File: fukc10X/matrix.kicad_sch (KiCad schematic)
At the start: 232 parts

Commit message: Extended Matrix. Added split r-shift and split l-shift. LED support. Removed three of the 4 top right keys because ugly and to make space for indicator leds there
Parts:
- removed D18, D19, D20: D_Small, Diode_SMD:D_SOD-123, symbol Device:D_Small
- removed MX17, MX18, MX19: MX_SW_solder, PCM_marbastlib-mx:SW_MX_1u, symbol PCM_marbastlib-mx:MX_SW_solder
- added D111, D99: D_Small, Diode_SMD:D_SOD-123, symbol Device:D_Small
- added MX115: MX_SW_solder, PCM_marbastlib-mx:SW_MX_1.25u, symbol PCM_marbastlib-mx:MX_SW_solder
- added MX116, MX118: MX_SW_solder, PCM_marbastlib-mx:SW_MX_1u, symbol PCM_marbastlib-mx:MX_SW_solder
- added MX117: MX_SW_solder, PCM_marbastlib-mx:SW_MX_1.75u, symbol PCM_marbastlib-mx:MX_SW_solder
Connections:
- net COL0: now also MX115.1
- net COL10: no longer MX104.1
- net COL11: now also MX104.1, MX116.1; no longer MX105.1
- net COL12: now also MX105.1, MX93.1, MX117.1
- net COL13: now also MX118.1; no longer MX93.1
- net COL6: no longer MX103.1
- net COL7: now also MX103.1
- net ROW4: now also D111.1 (K), D99.1 (K)
- net at D94.2 (A), MX93.2: now also MX117.2
- net at D83.2 (A), MX82.2: now also MX115.2
- new net: D111.2 (A), MX118.2
- new net: D99.2 (A), MX116.2
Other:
- moved on the sheet: D104, D78, MX103, MX77, S1

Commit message: Diodes moved, ISO enter added, Som Silkscreens moved aswell. Generally some cleanup
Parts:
- added D123: D_Small, Diode_SMD:D_SOD-123, symbol Device:D_Small
- added MX119, MX120: MX_SW_solder, PCM_marbastlib-mx:SW_MX_1u, symbol PCM_marbastlib-mx:MX_SW_solder
- added S9: MX_stab, PCM_marbastlib-mx:STAB_MX_ISO, symbol PCM_marbastlib-mx:MX_stab
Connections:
- net COL12: now also MX119.1
- net COL13: now also MX120.1
- net ROW3: now also D123.1 (K)
- net at D78.2 (A), MX77.2: now also MX120.2
- new net: D123.2 (A), MX119.2

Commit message: added split backspace + some updates to the matrix
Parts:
- removed D78: D_Small, Diode_SMD:D_SOD-123, symbol Device:D_Small
- added D124: D_Small, Diode_SMD:D_SOD-123, symbol Device:D_Small
- added MX121, MX122: MX_SW_solder, PCM_marbastlib-mx:SW_MX_1u, symbol PCM_marbastlib-mx:MX_SW_solder
- D10, D100, D101, D102, D103, D104, D105, D106, D107, D108, D109, D11, D110, D111, D112, D113, D114, D115, D12, D123, D13, D14, D15, D16, D17, D2, D21, D22, D23, D24, D25, D26, D27, D28, D29, D3, D30, D31, D32, D33, D34, D35, D36, D37, D38, D39, D4, D40, D41, D42, D43, D44, D45, D46, D47, D48, D49, D5, D50, D51, D52, D53, D54, D55, D56, D57, D58, D59, D6, D60, D61, D62, D64, D65, D67, D68, D69, D7, D70, D71, D72, D73, D74, D75, D76, D77, D79, D8, D80, D81, D82, D83, D84, D85, D86, D87, D88, D89, D9, D90, D91, D92, D93, D94, D95, D96, D97, D98, D99: LCSC (none) -> C81598
- S9: footprint PCM_marbastlib-mx:STAB_MX_ISO -> PCM_marbastlib-mx:STAB_MX_ISO-ROT
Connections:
- net COL12: now also MX77.1
- net COL13: now also MX121.1, MX122.1; no longer MX77.1
- net ROW3: now also D124.1 (K)
- net at D56.2 (A), MX55.2: now also MX120.2
- net at MX77.2: now also D123.2 (A), MX119.2; no longer MX120.2
- net at D35.2 (A), MX34.2: now also MX121.2
- new net: D124.2 (A), MX122.2
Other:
- moved on the sheet: MX120, MX77, S5

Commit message: silkscreen adjustment. 87U bottom row with 6u spacebar added.
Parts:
- added D125: D_Small, Diode_SMD:D_SOD-123, symbol Device:D_Small
- added MX123: MX_SW_solder, PCM_marbastlib-mx:SW_MX_1.5u, symbol PCM_marbastlib-mx:MX_SW_solder
- added MX124, MX125: MX_SW_solder, PCM_marbastlib-mx:SW_MX_1u, symbol PCM_marbastlib-mx:MX_SW_solder
- added S10: MX_stab, PCM_marbastlib-mx:STAB_MX_6u, symbol PCM_marbastlib-mx:MX_stab
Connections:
- net COL10: now also MX123.1
- net COL11: now also MX124.1
- net COL7: now also MX125.1
- net ROW5: now also D125.1 (K)
- net at D105.2 (A), MX104.2: now also MX124.2
- net at D104.2 (A), MX103.2: now also MX125.2
- new net: D125.2 (A), MX123.2
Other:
- moved on the sheet: S2

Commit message: adjusted spare diodes and some rounting. Updated step and production files
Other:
- moved on the sheet: S10
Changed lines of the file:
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@@
 	)
 	(junction
-		(at 41.91 130.81)
-		(diameter 0)
-		(color 0 0 0 0)
-	)
-	(junction
 		(at 120.65 33.02)
 		(diameter 0)
@@
 	)
 	(junction
-		(at 64.77 125.73)
-		(diameter 0)
-		(color 0 0 0 0)
-	)
-	(junction
 		(at 299.72 100.33)
 		(diameter 0)
@@
 	)
 	(junction
-		(at 36.83 125.73)
-		(diameter 0)
-		(color 0 0 0 0)
-	)
-	(junction
 		(at 111.76 118.11)
 		(diameter 0)
@@
 	)
 	(junction
-		(at 50.8 125.73)
-		(diameter 0)
-		(color 0 0 0 0)
-	)
-	(junction
 		(at 162.56 90.17)
 		(diameter 0)
@@
 	)
 	(junction
-		(at 181.61 130.81)
-		(diameter 0)
-		(color 0 0 0 0)
-	)
-	(junction
 		(at 153.67 100.33)
 		(diameter 0)
@@
 	)
 	(junction
-		(at 209.55 130.81)
-		(diameter 0)
-		(color 0 0 0 0)
-	)
-	(junction
 		(at 195.58 64.77)
 		(diameter 0)
@@
 	)
 	(junction
-		(at 218.44 125.73)
-		(diameter 0)
-		(color 0 0 0 0)
-	)
-	(junction
 		(at 176.53 33.02)
 		(diameter 0)
@@
 	)
 	(junction
-		(at 223.52 130.81)
-		(diameter 0)
-		(color 0 0 0 0)
-	)
-	(junction
 		(at 134.62 72.39)
 		(diameter 0)
@@
 	)
 	(junction
-		(at 55.88 130.81)
-		(diameter 0)
-		(color 0 0 0 0)
-	)
-	(junction
 		(at 190.5 107.95)
 		(diameter 0)
@@
 	)
 	(junction
-		(at 176.53 125.73)
-		(diameter 0)
-		(color 0 0 0 0)
-	)
-	(junction
 		(at 294.64 107.95)
 		(diameter 0)
@@
 	)
 	(junction
-		(at 69.85 130.81)
-		(diameter 0)
-		(color 0 0 0 0)
-	)
-	(junction
 		(at 270.51 33.02)
 		(diameter 0)
@@
 	)
 	(junction
-		(at 204.47 125.73)
-		(diameter 0)
-		(color 0 0 0 0)
-	)
-	(junction
 		(at 83.82 64.77)
 		(diameter 0)
@@
 	(wire
 		(pts
-			(xy 55.88 130.81) (xy 62.23 130.81)
-		)
-		(stroke
-			(width 0)
-			(type default)
-		)
-	)
-	(wire
-		(pts
 			(xy 139.7 64.77) (xy 153.67 64.77)
 		)
@@
 	(wire
 		(pts
-			(xy 176.53 130.81) (xy 181.61 130.81)
-		)
-		(stroke
-			(width 0)
-			(type default)
-		)
-	)
-	(wire
-		(pts
 			(xy 190.5 54.61) (xy 190.5 72.39)
 		)
@@
 	(wire
 		(pts
-			(xy 190.5 130.81) (xy 195.58 130.81)
-		)
-		(stroke
-			(width 0)
-			(type default)
-		)
-	)
-	(wire
-		(pts
 			(xy 313.69 82.55) (xy 327.66 82.55)
 		)
@@
 	(wire
 		(pts
-			(xy 171.45 125.73) (xy 176.53 125.73)
-		)
-		(stroke
-			(width 0)
-			(type default)
-		)
-	)
-	(wire
-		(pts
 			(xy 190.5 125.73) (xy 196.85 125.73)
 		)
@@
 	(wire
 		(pts
-			(xy 223.52 130.81) (xy 229.87 130.81)
-		)
-		(stroke
-			(width 0)
-			(type default)
-		)
-	)
-	(wire
-		(pts
 			(xy 167.64 82.55) (xy 181.61 82.55)
 		)
@@
 	(wire
 		(pts
-			(xy 209.55 130.81) (xy 215.9 130.81)
-		)
-		(stroke
-			(width 0)
-			(type default)
-		)
-	)
-	(wire
-		(pts
 			(xy 36.83 21.59) (xy 36.83 33.02)
 		)
@@
 	(wire
 		(pts
-			(xy 204.47 125.73) (xy 210.82 125.73)
-		)
-		(stroke
-			(width 0)
-			(type default)
-		)
-	)
-	(wire
-		(pts
 			(xy 299.72 64.77) (xy 313.69 64.77)
 		)
@@
 	(wire
 		(pts
-			(xy 50.8 125.73) (xy 57.15 125.73)
-		)
-		(stroke
-			(width 0)
-			(type default)
-		)
-	)
-	(wire
-		(pts
 			(xy 64.77 72.39) (xy 64.77 90.17)
 		)
@@
 	(wire
 		(pts
-			(xy 64.77 125.73) (xy 71.12 125.73)
-		)
-		(stroke
-			(width 0)
-			(type default)
-		)
-	)
-	(wire
-		(pts
 			(xy 204.47 107.95) (xy 204.47 125.73)
 		)
@@
 	(wire
 		(pts
-			(xy 127 125.73) (xy 134.62 125.73)
-		)
-		(stroke
-			(width 0)
-			(type default)
-		)
-	)
-	(wire
-		(pts
 			(xy 242.57 21.59) (xy 242.57 33.02)
 		)
@@
 	(wire
 		(pts
-			(xy 218.44 125.73) (xy 224.79 125.73)
-		)
-		(stroke
-			(width 0)
-			(type default)
-		)
-	)
-	(wire
-		(pts
 			(xy 64.77 90.17) (xy 64.77 107.95)
 		)
@@
 	(wire
 		(pts
-			(xy 69.85 130.81) (xy 76.2 130.81)
-		)
-		(stroke
-			(width 0)
-			(type default)
-		)
-	)
-	(wire
-		(pts
 			(xy 162.56 72.39) (xy 162.56 90.17)
 		)
@@
 	(wire
 		(pts
-			(xy 185.42 125.73) (xy 190.5 125.73)
-		)
-		(stroke
-			(width 0)
-			(type default)
-		)
-	)
-	(wire
-		(pts
 			(xy 195.58 82.55) (xy 209.55 82.55)
 		)
@@
 	(wire
 		(pts
-			(xy 132.08 130.81) (xy 139.7 130.81)
-		)
-		(stroke
-			(width 0)
-			(type default)
-		)
-	)
-	(wire
-		(pts
 			(xy 181.61 82.55) (xy 195.58 82.55)
 		)
@@
 	(wire
 		(pts
-			(xy 41.91 130.81) (xy 46.99 130.81)
-		)
-		(stroke
-			(width 0)
-			(type default)
-		)
-	)
-	(wire
-		(pts
 			(xy 55.88 135.89) (xy 69.85 135.89)
 		)
@@
 	(wire
 		(pts
-			(xy 36.83 125.73) (xy 41.91 125.73)
-		)
-		(stroke
-			(width 0)
-			(type default)
-		)
-	)
-	(wire
-		(pts
 			(xy 83.82 64.77) (xy 97.79 64.77)
 		)
@@
 	(symbol
 		(lib_id "PCM_marbastlib-mx:MX_stab")
-		(at 152.4 146.05 0)
+		(at 118.11 128.27 0)
 		(unit 1)
 		(body_style 1)
@@
 		(fields_autoplaced yes)
 		(property "Reference" "S10"
-			(at 158.75 144.6529 0)
+			(at 124.46 126.8729 0)
 			(show_name no)
 			(do_not_autoplace no)
@@
 		)
 		(property "Value" "MX_stab"
-			(at 158.75 147.1929 0)
+			(at 124.46 129.4129 0)
 			(show_name no)
 			(do_not_autoplace no)
@@
 		)
 		(property "Footprint" "PCM_marbastlib-mx:STAB_MX_6u"
-			(at 152.4 146.05 0)
+			(at 118.11 128.27 0)
 			(hide yes)
 			(show_name no)
@@
 		)
 		(property "Datasheet" ""
-			(at 152.4 146.05 0)
+			(at 118.11 128.27 0)
 			(hide yes)
 			(show_name no)
@@
 		)
 		(property "Description" "Cherry MX-style stabilizer"
-			(at 152.4 146.05 0)
+			(at 118.11 128.27 0)
 			(hide yes)
 			(show_name no)

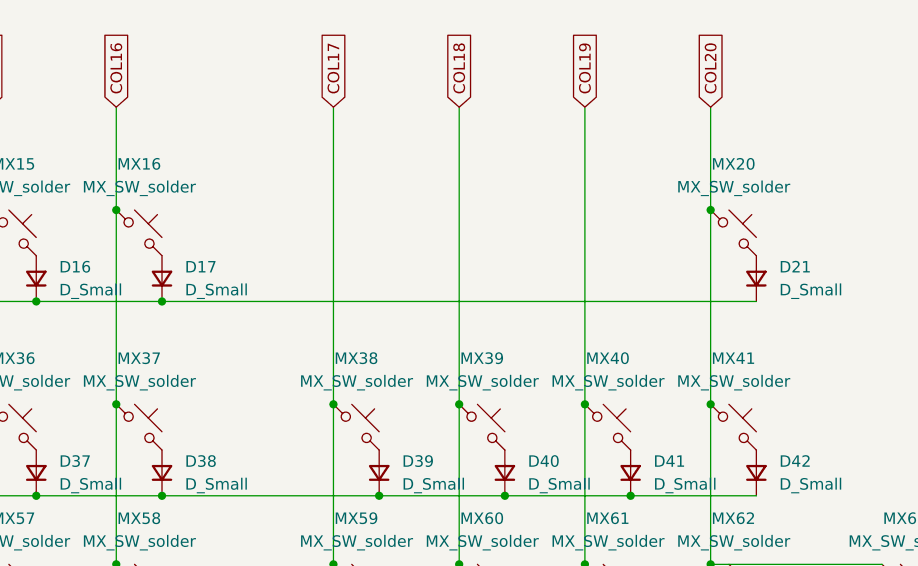
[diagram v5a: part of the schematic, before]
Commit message: added back keys above numpad + updated step file/prod stuff
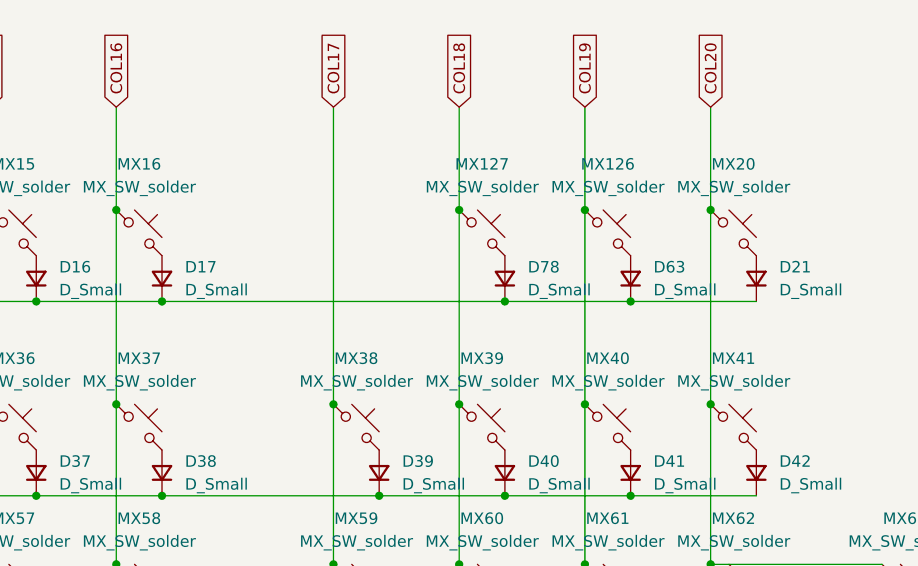
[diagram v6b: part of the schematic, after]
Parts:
- added D63, D78: D_Small, Diode_SMD:D_SOD-123, symbol Device:D_Small
- added MX126, MX127: MX_SW_solder, PCM_marbastlib-mx:SW_MX_1u, symbol PCM_marbastlib-mx:MX_SW_solder
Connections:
- net COL18: now also MX127.1
- net COL19: now also MX126.1
- net ROW0: now also D63.1 (K), D78.1 (K)
- new net: D78.2 (A), MX127.2
- new net: D63.2 (A), MX126.2
